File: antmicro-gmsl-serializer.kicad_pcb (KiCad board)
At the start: 4 copper layers, 91 parts, among them J1 Conn_FFC_WE_68715014022, J2 Conn_FAKRA_2FAI-NZSP-PCBB6, U1 AP62301_TSOT, U2 AP62301_TSOT, U3 NCP163ASN330T1G, U4 REF3025AIDBZT, U5 TLV73312PDBVT, U6 MAX9295A, Y1 Resonator_25MHz_ABM8G

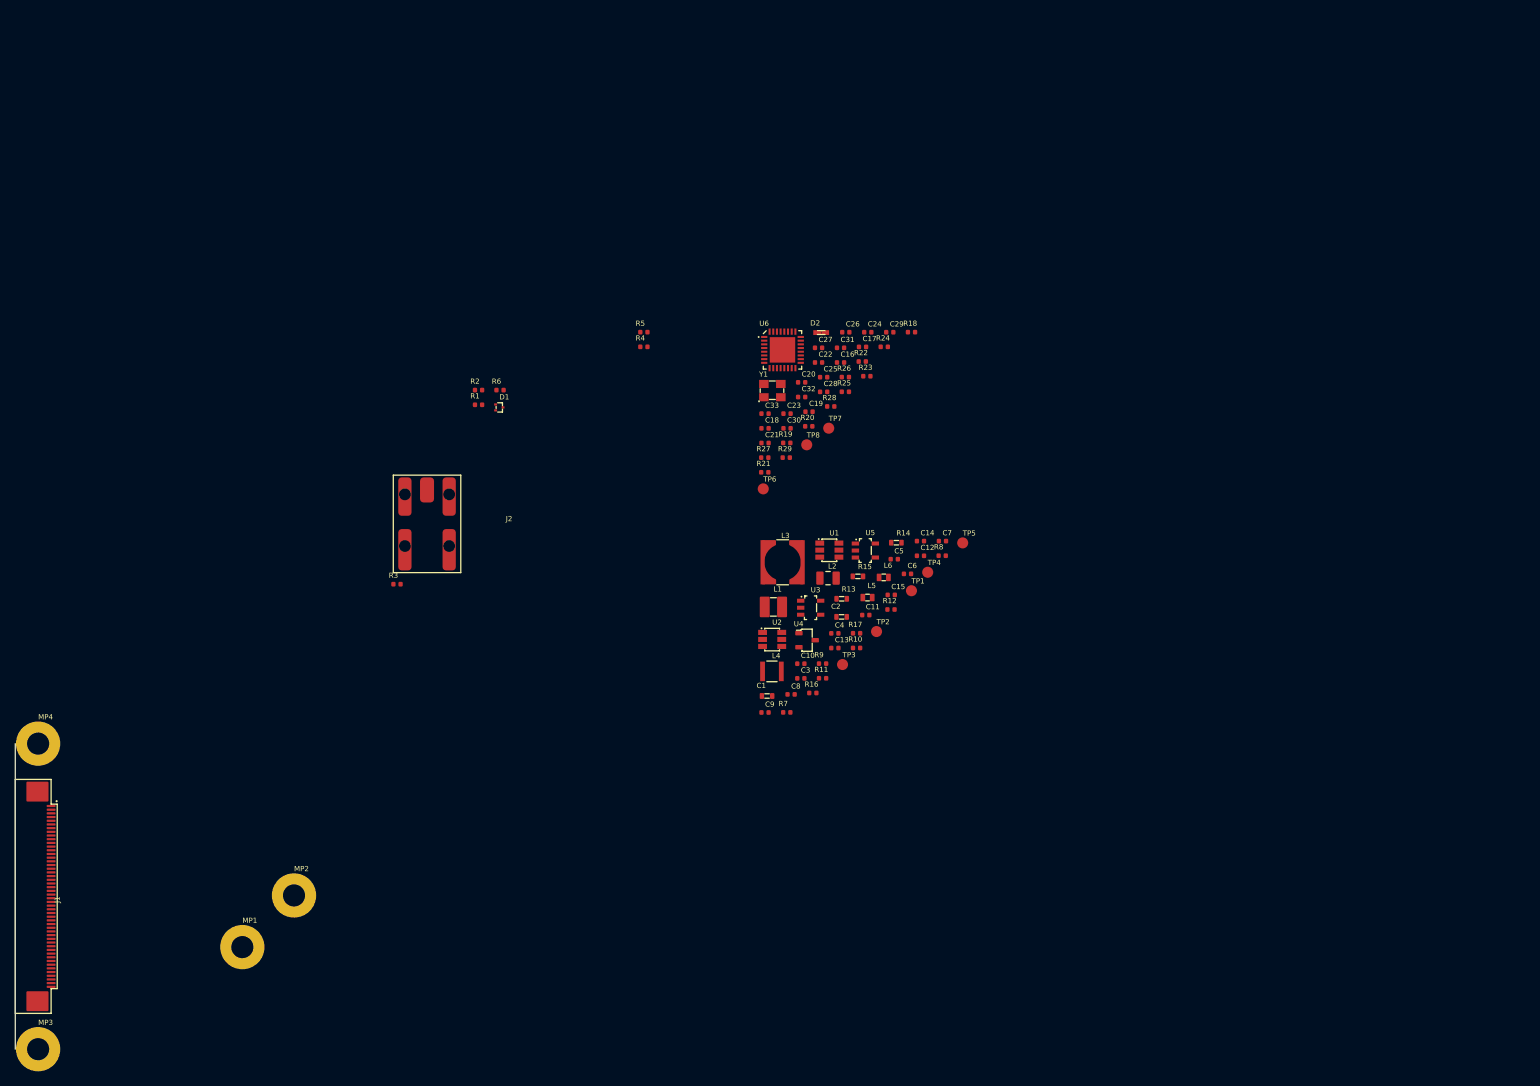
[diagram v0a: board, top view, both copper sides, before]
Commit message: Draw board outline, place MPs and 50pin conn
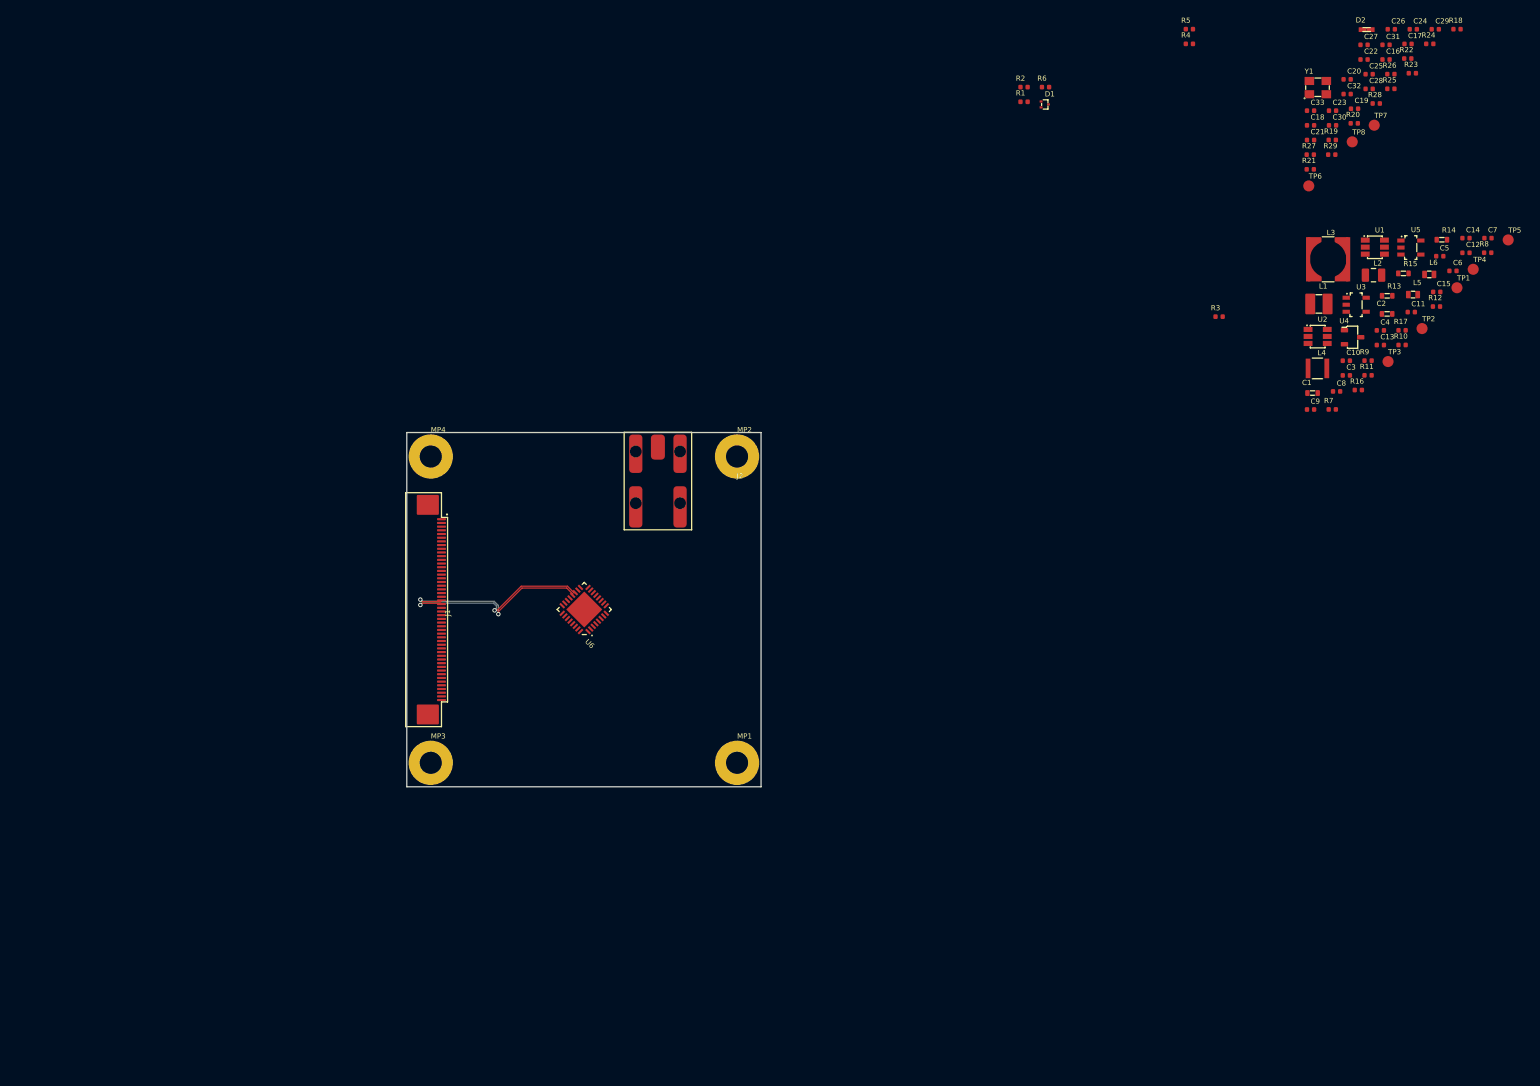
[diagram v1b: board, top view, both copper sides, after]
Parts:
- moved R3 117.1 mm to (233.7, 62.1)
- moved C12 84.5 mm to (267.2, 53.5)
- moved C14 84.5 mm to (267.2, 51.5)
- moved C2 84.5 mm to (256.5, 61.8)
- moved C23 84.5 mm to (249.1, 34.2)
- moved C26 84.5 mm to (257.0, 23.2)
- moved C30 84.5 mm to (249.1, 36.2)
- moved C5 84.5 mm to (263.6, 54.0)
- moved D2 84.5 mm to (253.7, 23.3)
- moved L1 84.5 mm to (247.2, 60.4)
- moved L3 84.5 mm to (248.5, 54.4)
- moved L5 84.5 mm to (260.0, 59.2)
- moved R12 84.5 mm to (263.2, 60.8)
- moved R13 84.5 mm to (256.5, 59.3)
- moved R25 84.5 mm to (257.0, 31.3)
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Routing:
- net CSI0_D1_N: track 0.00 -> 27.3 mm, vias 0 -> 2
- net CSI0_D1_P: track 0.00 -> 26.9 mm, vias 0 -> 2
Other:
- board outline added: 48 x 48 mm

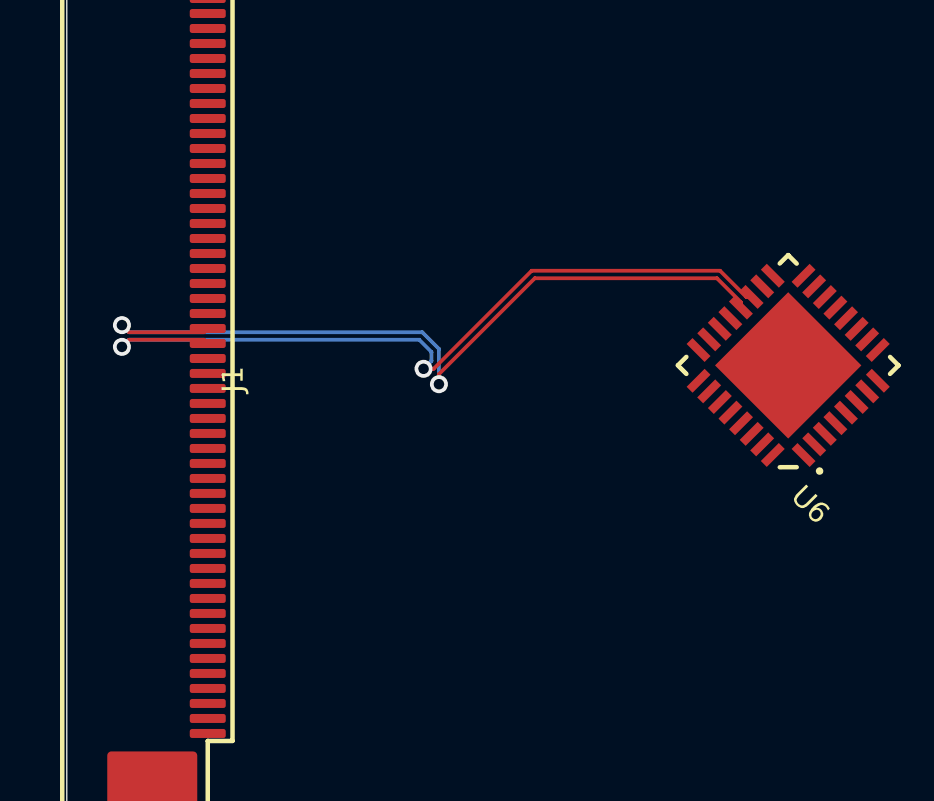
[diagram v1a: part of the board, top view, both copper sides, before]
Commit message: Route CSI lines
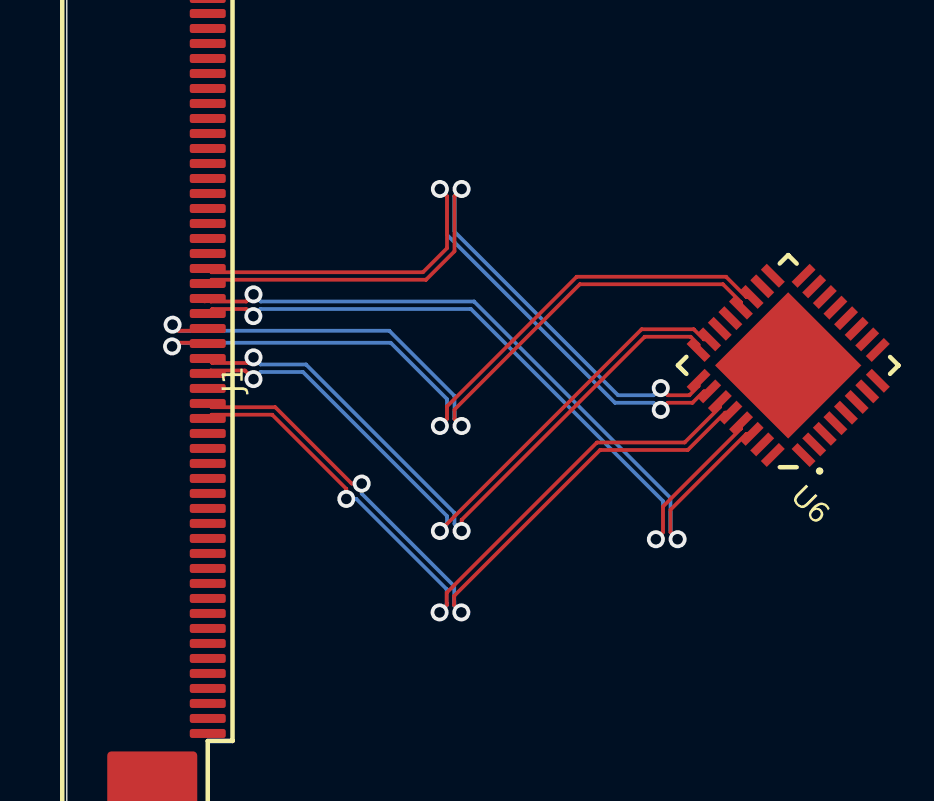
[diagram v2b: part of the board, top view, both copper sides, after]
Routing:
- net CSI1_D0_N: track 0.00 -> 24.8 mm, vias 0 -> 2
- net CSI1_D0_P: track 0.00 -> 24.6 mm, vias 0 -> 2
- net CSI0_CLK_N: track 0.00 -> 24.5 mm, vias 0 -> 2
- net CSI0_CLK_P: track 0.00 -> 24.1 mm, vias 0 -> 2
- net CSI1_D1_N: track 0.00 -> 23.5 mm, vias 0 -> 2
- net CSI1_D1_P: track 0.00 -> 23.3 mm, vias 0 -> 2
- net CSI0_D0_P: track 0.00 -> 22.7 mm, vias 0 -> 2
- net CSI0_D0_N: track 0.00 -> 22.3 mm, vias 0 -> 2
- net CSI0_D1_N: track 27.3 -> 25.1 mm
- net CSI0_D1_P: track 26.9 -> 25.2 mm

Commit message: Tune CSI lines
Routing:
- net CSI0_D0_N: track 22.3 -> 25.2 mm
- net CSI0_D0_P: track 22.7 -> 25.1 mm
- net CSI1_D1_P: track 23.3 -> 25.3 mm
- net CSI1_D1_N: track 23.5 -> 25.2 mm
- net CSI0_CLK_P: track 24.1 -> 25.3 mm
- net CSI1_D0_P: track 24.6 -> 25.5 mm
- net CSI0_CLK_N: track 24.5 -> 25.3 mm
- net CSI1_D0_N: track 24.8 -> 25.5 mm
